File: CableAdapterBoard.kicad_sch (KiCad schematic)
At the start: 15 parts, among them J1 IPL1-104-01-L-D-K, J2 IPL1-105-01-L-D-K, J21 1888174-6, J3 IPL1-105-01-X-D-K, J31 1888174-6

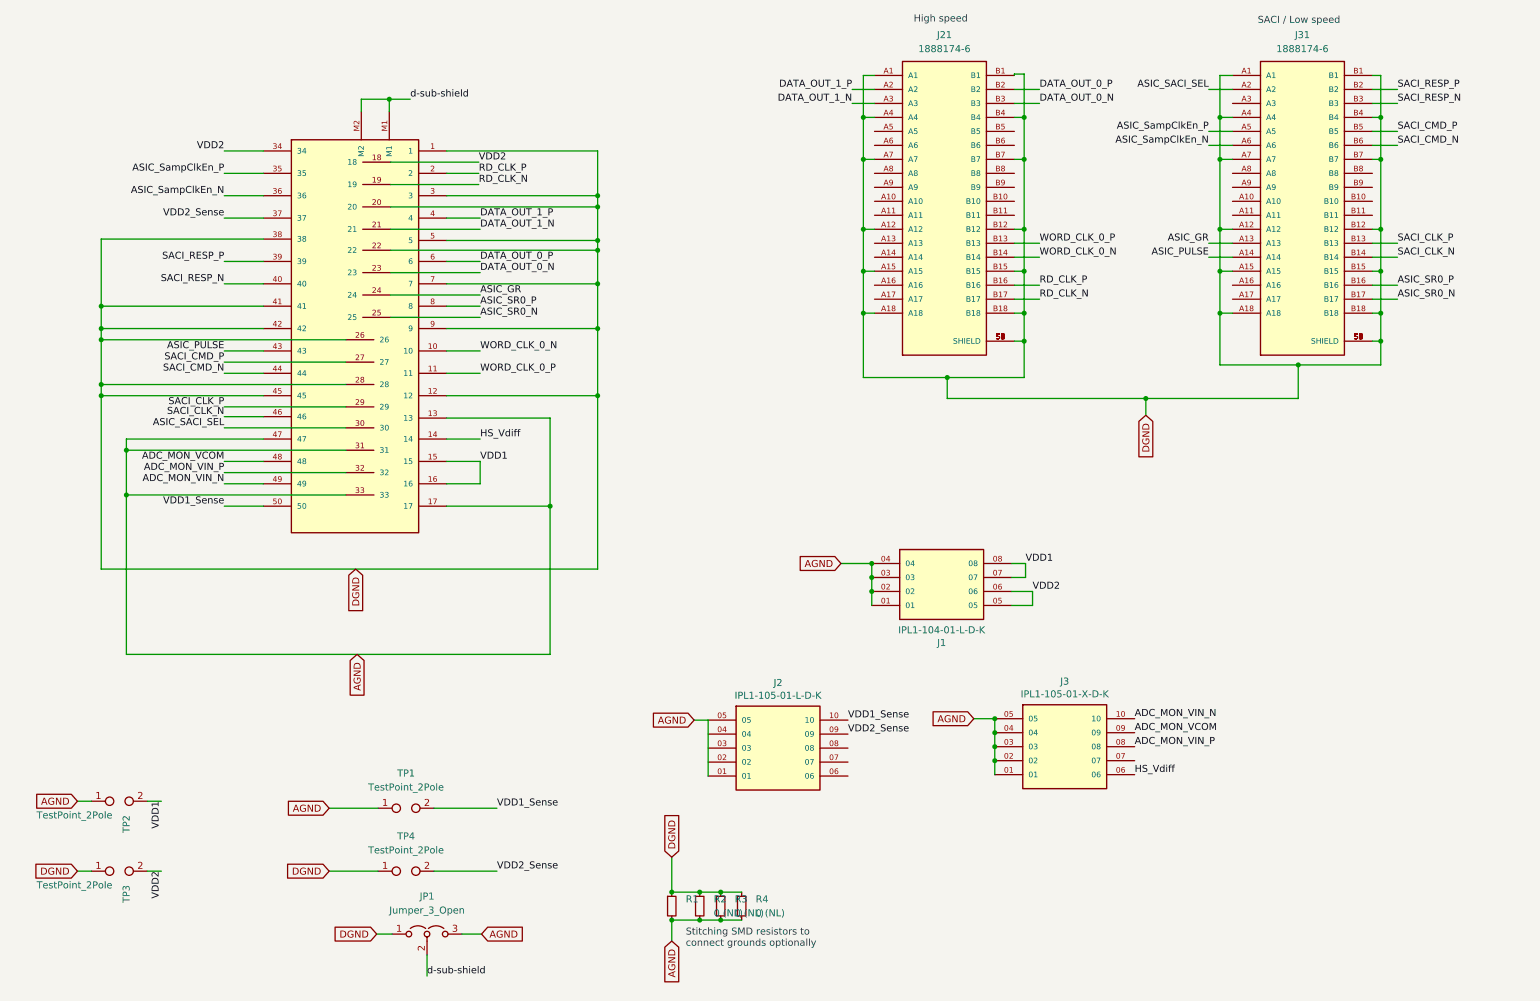
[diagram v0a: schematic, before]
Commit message: Changed orientation of 36 pin minisas connectors to be CORRECT. old version needed a flip due to always top-to-bottom crossover format of these cables. corrected some labeling.
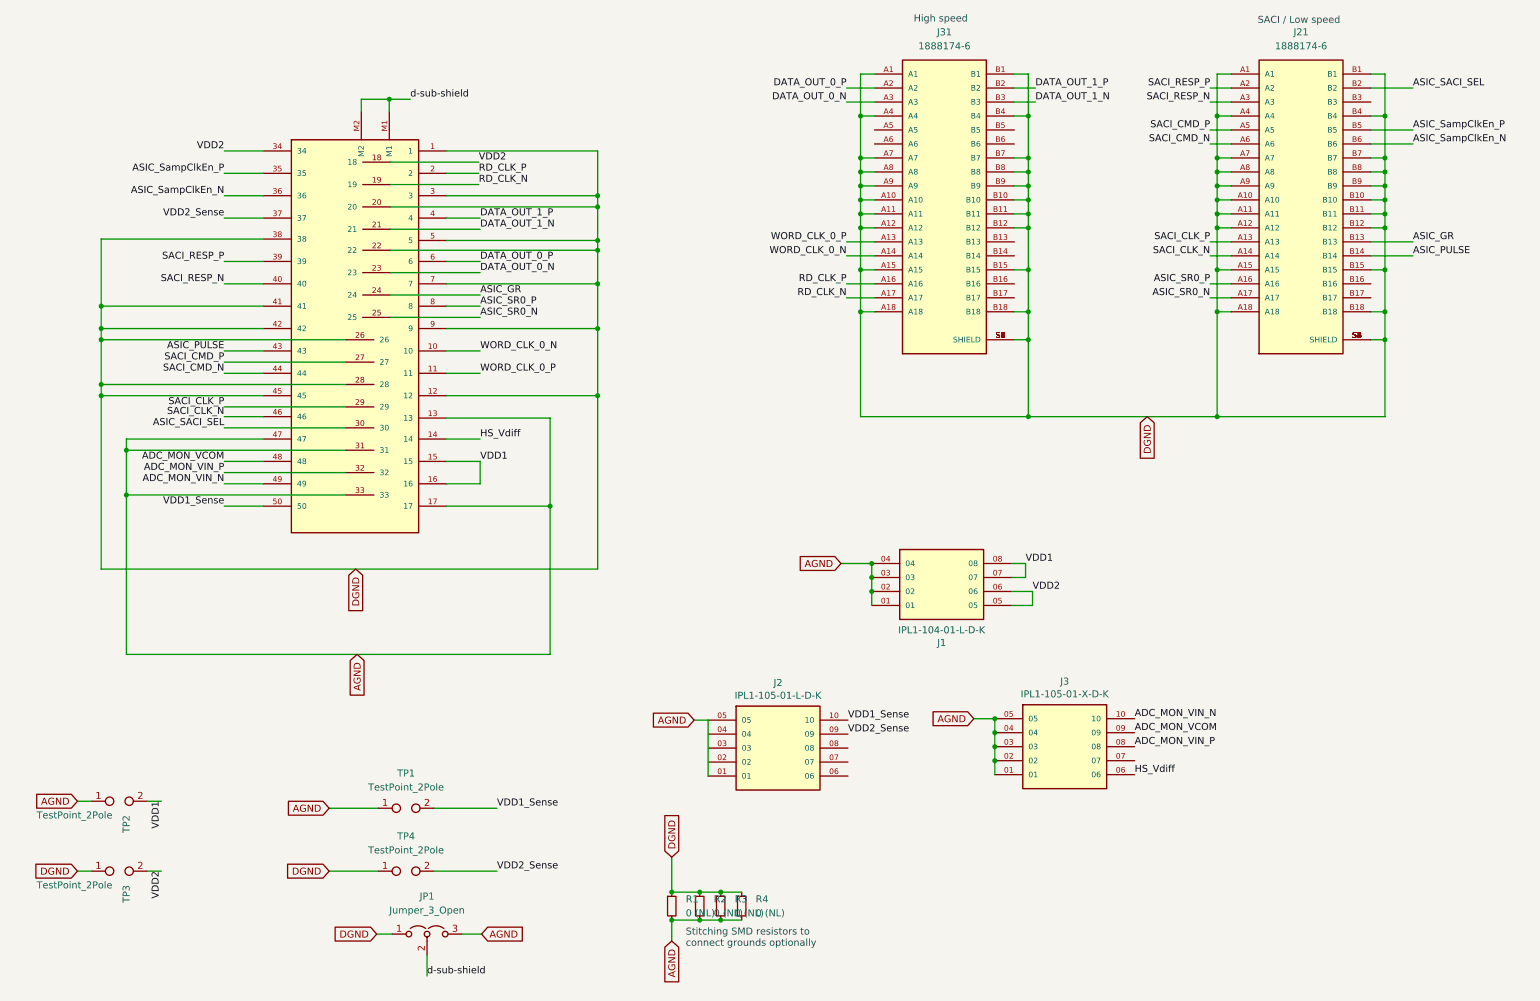
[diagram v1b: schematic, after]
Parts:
- DSUB1: footprint SKT-50 -> Connector_Dsub:SKT-50
- J21: renamed from J31; footprint Connector:TE_1888174-6 -> Tiles:TE_1888174-6
- J31: renamed from J21; footprint Connector:TE_1888174-6 -> Tiles:TE_1888174-6
- R1: value (none) -> 0 (NL); footprint (none) -> Resistor_SMD:R_0805_2012Metric_Pad1.20x1.40mm_HandSolder
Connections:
- net ASIC_GR: now also J21.B13; no longer J21.A13
- net ASIC_PULSE: now also J21.B14; no longer J21.A14
- net ASIC_SACI_SEL: now also J21.B2; no longer J21.A2
- net ASIC_SR0_N: now also J21.A17; no longer J21.B17
- net ASIC_SR0_P: now also J21.A16; no longer J21.B16
- net ASIC_SampClkEn_N: now also J21.B6; no longer J21.A6
- net ASIC_SampClkEn_P: now also J21.B5; no longer J21.A5
- net DATA_OUT_0_N: now also J31.A3; no longer J31.B3
- net DATA_OUT_0_P: now also J31.A2; no longer J31.B2
- net DATA_OUT_1_N: now also J31.B3; no longer J31.A3
- net DATA_OUT_1_P: now also J31.B2; no longer J31.A2
- net DGND: now also J21.A10, J21.A11, J21.A8, J21.A9, J21.B10, J21.B11, J21.B8, J21.B9, J31.A10, J31.A11, J31.A8, J31.A9, J31.B10, J31.B11, J31.B8, J31.B9
- net RD_CLK_N: now also J31.A17; no longer J31.B17
- net RD_CLK_P: now also J31.A16; no longer J31.B16
- net SACI_CLK_N: now also J21.A14; no longer J21.B14
- net SACI_CLK_P: now also J21.A13; no longer J21.B13
- net SACI_CMD_N: now also J21.A6; no longer J21.B6
- net SACI_CMD_P: now also J21.A5; no longer J21.B5
- net SACI_RESP_N: now also J21.A3; no longer J21.B3
- net SACI_RESP_P: now also J21.A2; no longer J21.B2
- net WORD_CLK_0_N: now also J31.A14; no longer J31.B14
- net WORD_CLK_0_P: now also J31.A13; no longer J31.B13
